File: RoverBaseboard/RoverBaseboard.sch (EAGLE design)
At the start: 60 parts, among them IC1 7805, IC3 3.3V, U2 microSD

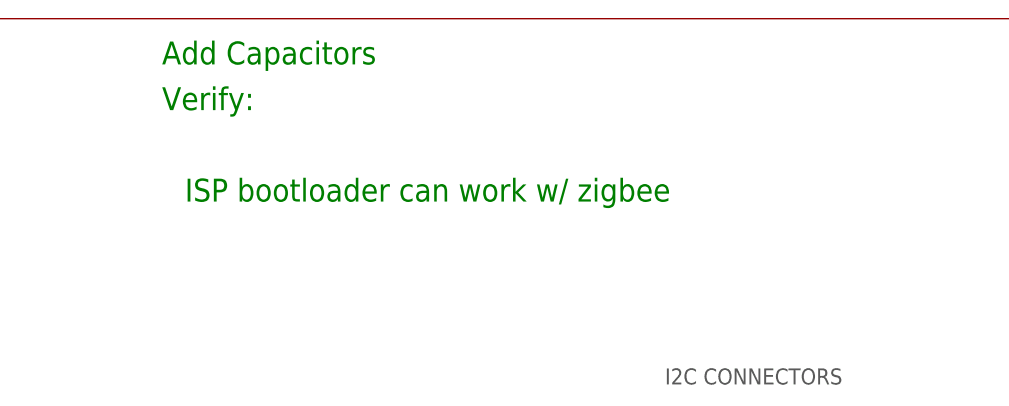
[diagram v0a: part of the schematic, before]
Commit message: Revised schematic after verifying several items. Renamed files.
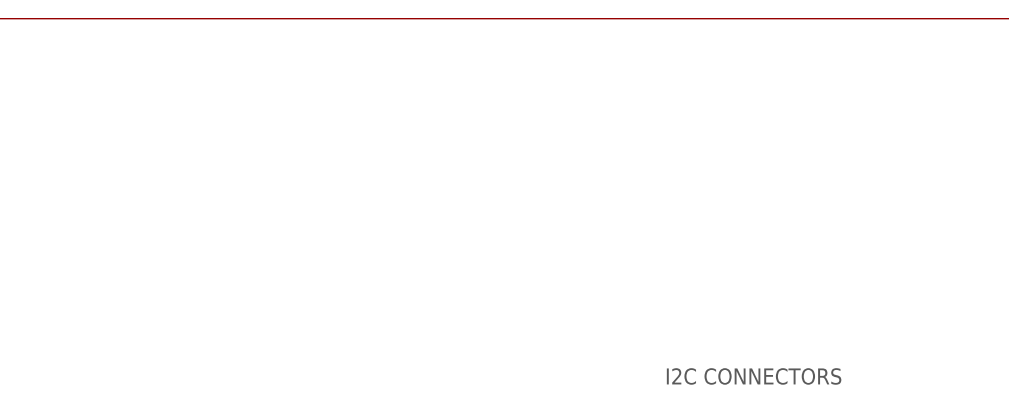
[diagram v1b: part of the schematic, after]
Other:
- note removed: "Add Capacitors"
- note removed: "ISP bootloader can work w/ zigbee"
- note removed: "Verify:"
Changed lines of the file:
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@@
 <wire x1="14.732" y1="141.224" x2="174.752" y2="141.224" width="0.1524" layer="97" style="shortdash"/>
 <text x="174.752" y="142.494" size="1.778" layer="97" rot="MR0">MBED</text>
-<text x="152.4" y="238.76" size="2.54" layer="91">Verify:</text>
-<text x="154.94" y="228.6" size="2.54" layer="91">ISP bootloader can work w/ zigbee</text>
-<text x="152.4" y="243.84" size="2.54" layer="91">Add Capacitors</text>
 <text x="14.732" y="142.24" size="1.778" layer="97">MBED</text>
 <wire x1="0" y1="248.92" x2="480.06" y2="248.92" width="0.1524" layer="94"/>

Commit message: Revised power hookup; 3.3V to 3.3V pin, disconnect EXT_POWER from 5V.
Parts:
- removed C1, C16: 470, bt_rcl:CAP_POL_SMC_C
- C17: value 470 -> 100; device bt_rcl:CAP_POL_SMC_C -> rcl:CPOL-US140CLH-0810
- C2, C3: value 470 -> 10; device bt_rcl:CAP_POL_SMC_C -> rcl:C-USC1206
- R1, R10, R2, R3, R4, R7, R8, R9: value 220 -> 10K
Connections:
- net +3V3: now also U$1.VOUT/3.3V; no longer C1.+, C16.+
- net +5V: now also C2.1, C3.1; no longer C2.+, C3.+, U$1.EXT_POWX
- net GND: now also C2.2, C3.2; no longer C1.-, C16.-, C2.-, C3.-
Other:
- note added: "0.6"
- note added: "Verify input cap values"
- note removed: "0.5"
- moved on the sheet: BECSEL, IC1
